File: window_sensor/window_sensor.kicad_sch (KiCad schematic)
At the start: 13 parts, among them J3 Screw_Terminal_01x02, J4 Conn_01x02, J6 Conn_ST_STDC14, U1 RFM69HW, U2 STM32G031K8Tx, Y1 32.768KHz

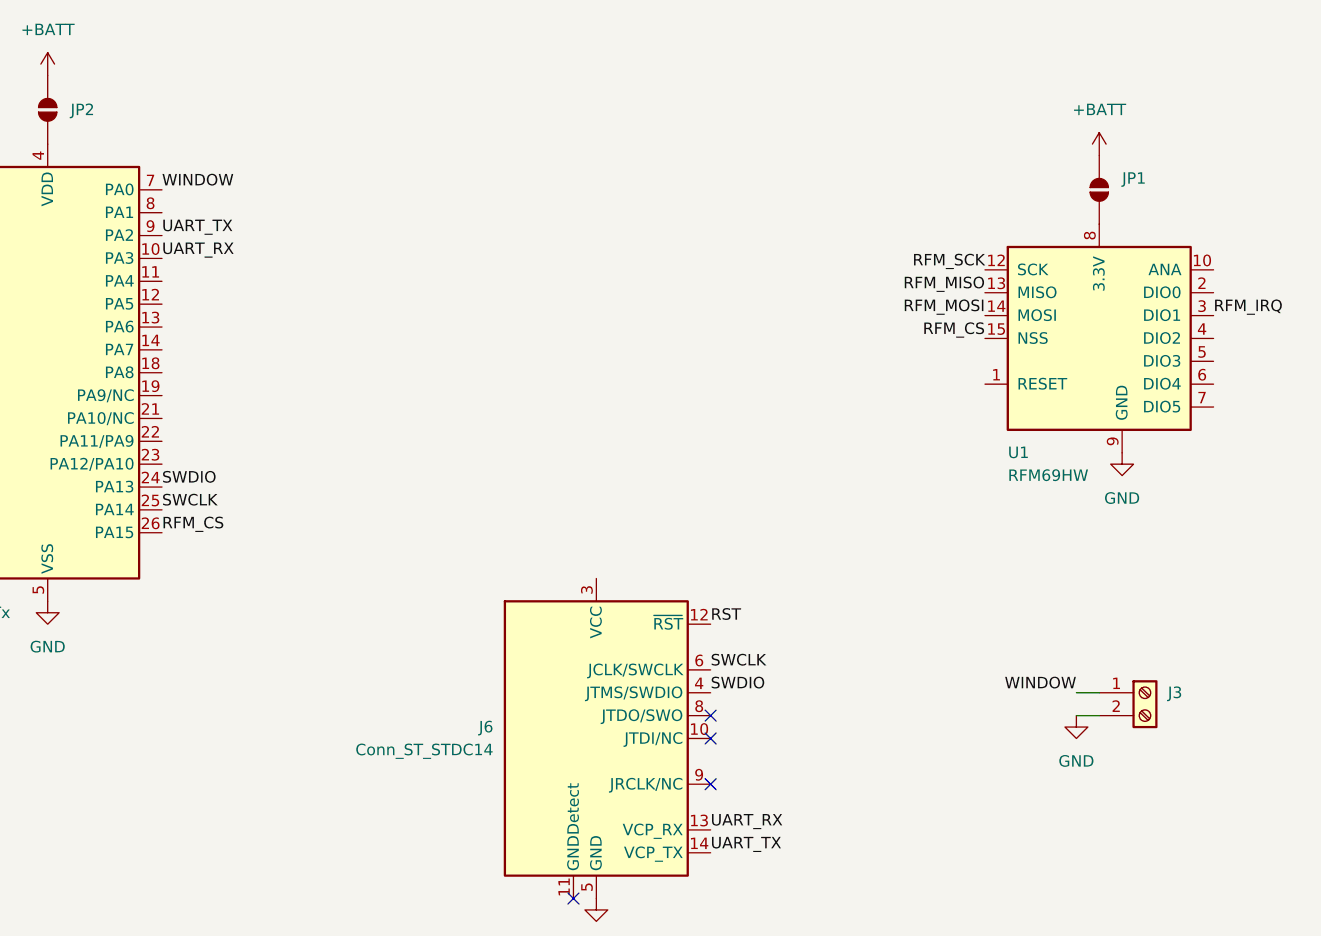
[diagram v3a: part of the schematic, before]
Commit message: optional external pull-up for sensor pin
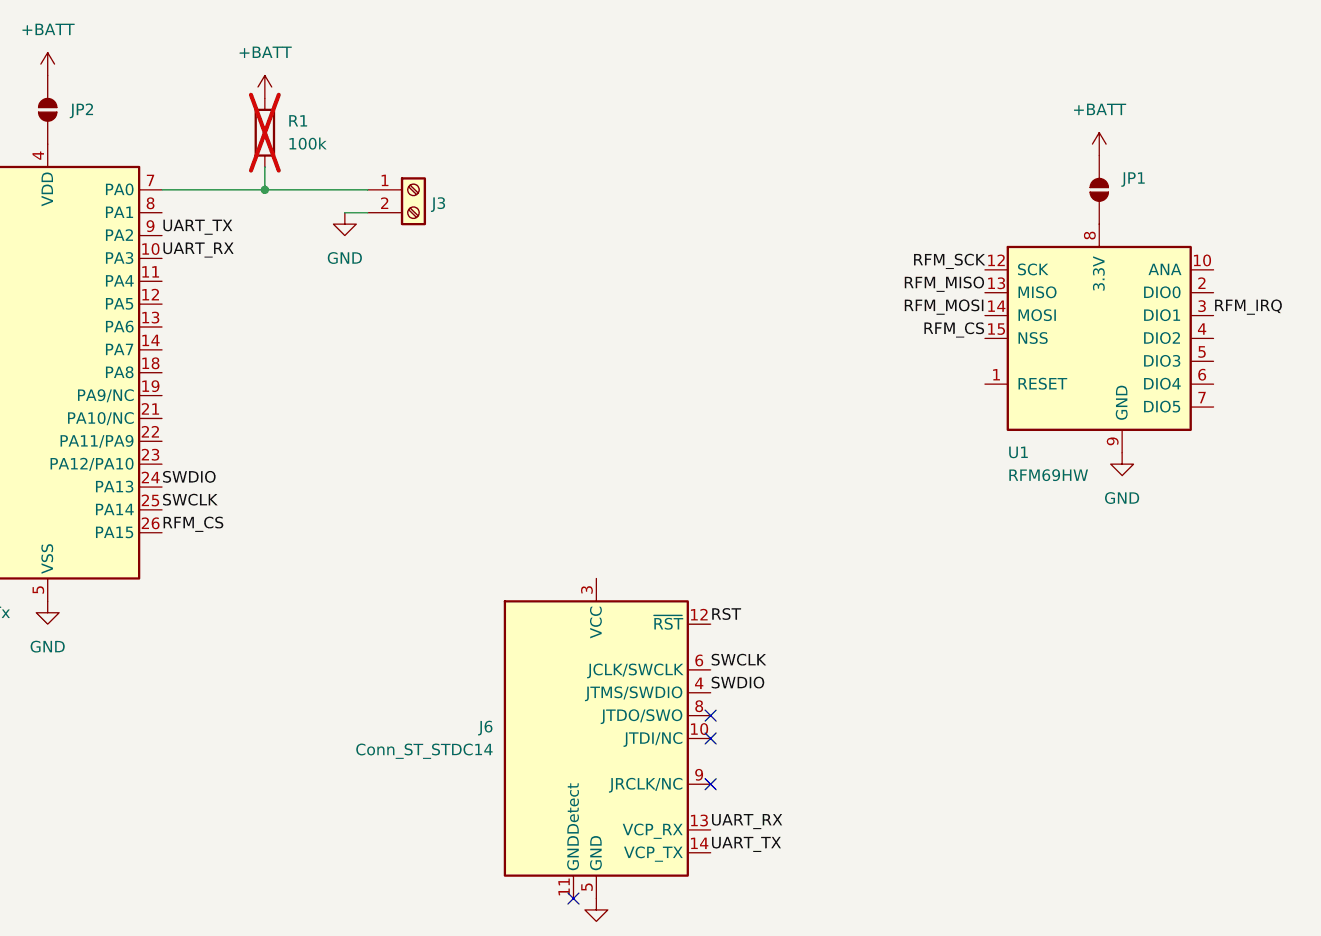
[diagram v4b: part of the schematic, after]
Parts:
- added R1: 100k, Resistor_SMD:R_0805_2012Metric_Pad1.20x1.40mm_HandSolder, symbol Device:R
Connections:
- net +BATT: now also R1.1
- net WINDOW: no longer names the net of J3.1 (Pin_1), U2.7 (PA0)
- net WINDOW: now also R1.2
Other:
- moved on the sheet: J3
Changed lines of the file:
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@@
 	(paper "A4")
+	(junction
+		(at 124.46 33.02)
+		(diameter 0)
+		(color 0 0 0 0)
+	)
 	(junction
 		(at 52.07 45.72)
@@
 	(wire
 		(pts
-			(xy 214.63 91.44) (xy 217.17 91.44)
+			(xy 133.35 35.56) (xy 135.89 35.56)
 		)
 		(stroke
@@
 	(wire
 		(pts
-			(xy 40.64 45.72) (xy 36.83 45.72)
+			(xy 124.46 30.48) (xy 124.46 33.02)
 		)
 		(stroke
@@
 	(wire
 		(pts
-			(xy 52.07 43.18) (xy 52.07 45.72)
+			(xy 40.64 45.72) (xy 36.83 45.72)
 		)
 		(stroke
@@
 	(wire
 		(pts
-			(xy 68.58 34.29) (xy 68.58 33.02)
+			(xy 52.07 43.18) (xy 52.07 45.72)
 		)
 		(stroke
@@
 	(wire
 		(pts
-			(xy 36.83 40.64) (xy 36.83 45.72)
+			(xy 124.46 33.02) (xy 135.89 33.02)
 		)
 		(stroke
@@
 	(wire
 		(pts
-			(xy 36.83 45.72) (xy 36.83 48.26)
+			(xy 68.58 34.29) (xy 68.58 33.02)
 		)
 		(stroke
@@
 	(wire
 		(pts
-			(xy 52.07 48.26) (xy 52.07 45.72)
+			(xy 36.83 40.64) (xy 36.83 45.72)
 		)
 		(stroke
@@
 	(wire
 		(pts
-			(xy 217.17 88.9) (xy 214.63 88.9)
+			(xy 36.83 45.72) (xy 36.83 48.26)
 		)
 		(stroke
@@
 	(wire
 		(pts
-			(xy 85.09 40.64) (xy 36.83 40.64)
+			(xy 52.07 48.26) (xy 52.07 45.72)
 		)
 		(stroke
@@
 		)
 	)
+	(wire
+		(pts
+			(xy 113.03 33.02) (xy 124.46 33.02)
+		)
+		(stroke
+			(width 0)
+			(type default)
+		)
+	)
+	(wire
+		(pts
+			(xy 85.09 40.64) (xy 36.83 40.64)
+		)
+		(stroke
+			(width 0)
+			(type default)
+		)
+	)
 	(label "RFM_MOSI"
 		(at 85.09 60.96 180)
@@
 		)
 	)
-	(label "WINDOW"
-		(at 214.63 88.9 180)
-		(fields_autoplaced yes)
-		(effects
-			(font
-				(size 1.27 1.27)
-			)
-			(justify right bottom)
-		)
-	)
 	(label "RFM_CS"
 		(at 204.47 49.53 180)
@@
 		)
 	)
-	(label "WINDOW"
-		(at 113.03 33.02 0)
-		(fields_autoplaced yes)
-		(effects
-			(font
-				(size 1.27 1.27)
-			)
-			(justify left bottom)
-		)
-	)
 	(label "SWDIO"
 		(at 173.99 88.9 0)
@@
 	(symbol
 		(lib_id "power:GND")
-		(at 214.63 91.44 0)
+		(at 133.35 35.56 0)
 		(unit 1)
 		(exclude_from_sim no)
@@
 		(fields_autoplaced yes)
 		(property "Reference" "#PWR014"
-			(at 214.63 97.79 0)
+			(at 133.35 41.91 0)
 			(effects
 				(font
@@
 		)
 		(property "Value" "GND"
-			(at 214.63 96.52 0)
+			(at 133.35 40.64 0)
 			(effects
 				(font
@@
 		)
 		(property "Footprint" ""
-			(at 214.63 91.44 0)
+			(at 133.35 35.56 0)
 			(effects
 				(font
@@
 		)
 		(property "Datasheet" ""
-			(at 214.63 91.44 0)
+			(at 133.35 35.56 0)
 			(effects
 				(font
@@
 		)
 		(property "Description" ""
-			(at 214.63 91.44 0)
+			(at 133.35 35.56 0)
 			(effects
 				(font
@@
 	(symbol
 		(lib_id "power:+BATT")
-		(at 55.88 20.32 0)
+		(at 124.46 22.86 0)
 		(unit 1)
 		(exclude_from_sim no)
@@
 		(dnp no)
 		(fields_autoplaced yes)
+		(property "Reference" "#PWR05"
+			(at 124.46 26.67 0)
+			(effects
+				(font
+					(size 1.27 1.27)
+				)
+				(hide yes)
+			)
+		)
+		(property "Value" "+BATT"
+			(at 124.46 17.78 0)
+			(effects
+				(font
+					(size 1.27 1.27)
+				)
+			)
+		)
+		(property "Footprint" ""
+			(at 124.46 22.86 0)
+			(effects
+				(font
+					(size 1.27 1.27)
+				)
+				(hide yes)
+			)
+		)
+		(property "Datasheet" ""
+			(at 124.46 22.86 0)
+			(effects
+				(font
+					(size 1.27 1.27)
+				)
+				(hide yes)
+			)
+		)
+		(property "Description" ""
+			(at 124.46 22.86 0)
+			(effects
+				(font
+					(size 1.27 1.27)
+				)
+				(hide yes)
+			)
+		)
+		(pin "1"
+		)
+		(instances
+			(project "window_sensor"
+				(path "/ab29af63-8a47-474a-b13c-fa0edfd1f1b4"
+					(reference "#PWR05")
+					(unit 1)
+				)
+			)
+		)
+	)
+	(symbol
+		(lib_id "power:+BATT")
+		(at 55.88 20.32 0)
+		(unit 1)
+		(exclude_from_sim no)
+		(in_bom yes)
+		(on_board yes)
+		(dnp no)
+		(fields_autoplaced yes)
 		(property "Reference" "#PWR010"
 			(at 55.88 24.13 0)
@@
 	)
 	(symbol
+		(lib_id "Device:R")
+		(at 124.46 26.67 0)
+		(unit 1)
+		(exclude_from_sim no)
+		(in_bom yes)
+		(on_board yes)
+		(dnp yes)
+		(fields_autoplaced yes)
+		(property "Reference" "R1"
+			(at 127 25.3999 0)
+			(effects
+				(font
+					(size 1.27 1.27)
+				)
+				(justify left)
+			)
+		)
+		(property "Value" "100k"
+			(at 127 27.9399 0)
+			(effects
+				(font
+					(size 1.27 1.27)
+				)
+				(justify left)
+			)
+		)
+		(property "Footprint" "Resistor_SMD:R_0805_2012Metric_Pad1.20x1.40mm_HandSolder"
+			(at 122.682 26.67 90)
+			(effects
+				(font
+					(size 1.27 1.27)
+				)
+				(hide yes)
+			)
+		)
+		(property "Datasheet" "~"
+			(at 124.46 26.67 0)
+			(effects
+				(font
+					(size 1.27 1.27)
+				)
+				(hide yes)
+			)
+		)
+		(property "Description" "Resistor"
+			(at 124.46 26.67 0)
+			(effects
+				(font
+					(size 1.27 1.27)
+				)
+				(hide yes)
+			)
+		)
+		(pin "1"
+		)
+		(pin "2"
+		)
+		(instances
+			(project ""
+				(path "/ab29af63-8a47-474a-b13c-fa0edfd1f1b4"
+					(reference "R1")
+					(unit 1)
+				)
+			)
+		)
+	)
+	(symbol
 		(lib_id "power:GND")
 		(at 83.82 114.3 0)
@@
 	(symbol
 		(lib_id "Connector:Screw_Terminal_01x02")
-		(at 222.25 88.9 0)
+		(at 140.97 33.02 0)
 		(unit 1)
 		(exclude_from_sim no)
@@
 		(dnp no)
 		(property "Reference" "J3"
-			(at 224.79 88.9 0)
+			(at 143.002 34.544 0)
 			(effects
 				(font
@@
 		)
 		(property "Value" "Screw_Terminal_01x02"
-			(at 224.79 91.44 0)
+			(at 143.51 35.56 0)
 			(effects
 				(font
@@
 		)
 		(property "Footprint" "TerminalBlock:TerminalBlock_Xinya_XY308-2.54-2P_1x02_P2.54mm_Horizontal"
-			(at 222.25 88.9 0)
+			(at 140.97 33.02 0)
 			(effects
 				(font
@@
 		)
 		(property "Datasheet" "~"
-			(at 222.25 88.9 0)
+			(at 140.97 33.02 0)
 			(effects
 				(font
@@
 		)
 		(property "Description" ""
-			(at 222.25 88.9 0)
-			(effects
-				(font
+			(at 140.97 33.02 0)
+			(effects
+				(font

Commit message: pcb updated
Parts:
- added AE1: Antenna_Shield, symbol Device:Antenna_Shield
- added C6: 100nF, Capacitor_SMD:C_0805_2012Metric_Pad1.18x1.45mm_HandSolder, symbol Device:C
- added R2: 0, Resistor_SMD:R_0805_2012Metric_Pad1.20x1.40mm_HandSolder, symbol Device:R
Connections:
- net +BATT: now also J6.3 (VCC), C6.1
- net GND: now also AE1.2 (Shield), C6.2
- net at U1.1 (RESET): now also R2.2
- net at U1.10 (ANA): now also AE1.1 (A)
- net RFM_RESET: now reaches U2.18 (PA8)
- net RFM_RESET: now also R2.1
- no-connect marks 4 -> 25
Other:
- moved on the sheet: C1, C2, C3, C4, C5, J3, J4, J6, JP1, JP2, R1, U1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

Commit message: First PCB
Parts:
- removed J4: Conn_01x02, Connector_PinHeader_2.54mm:PinHeader_1x02_P2.54mm_Vertical, symbol Connector_Generic:Conn_01x02
- removed R2: 0, Resistor_SMD:R_0805_2012Metric_Pad1.20x1.40mm_HandSolder, symbol Device:R
- added BT1: Battery, Battery:BatteryHolder_Keystone_2462_2xAA, symbol Device:Battery
- added JP3: SolderJumper_2_Bridged, Jumper:SolderJumper-2_P1.3mm_Open_TrianglePad1.0x1.5mm, symbol Jumper:SolderJumper_2_Open
- AE1: value Antenna_Shield -> Antenna; footprint (none) -> RF_Antenna:NiceRF_SW868-TH13_868Mhz; symbol Device:Antenna_Shield -> Device:Antenna
- J2: renamed from J6; footprint Connector_PinHeader_1.27mm:PinHeader_2x07_P1.27mm_Vertical_SMD -> Connector_PinHeader_1.27mm:PinHeader_2x07_P1.27mm_Horizontal; manf# (none) -> 20021112-00014T1LF
- renumbered C3 to C2, C2 to C3, C6 to C5, C5 to C6, J3 to J1, JP2 to JP1, JP1 to JP2, U2 to U1, U1 to U2
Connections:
- net +BATT: now also BT1.1 (+)
- net GND: now also BT1.2 (-); no longer AE1.2 (Shield)
- net RFM_RESET: now also U1.23 (PA12/PA10), JP3.2 (B); no longer U1.18 (PA8)
- net at U2.1 (RESET): now also JP3.1 (A)
- no-connect marks 25 -> 24
